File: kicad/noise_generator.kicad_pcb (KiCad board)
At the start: 2 copper layers, 57.2 x 38.1 mm, 12 parts, among them J1 Conn_Coaxial, J2 Connector, U1 LM741

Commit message: Adjustments
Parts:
- moved C1 76.5 mm to (130.4, 82.2)
- moved C2 76.5 mm to (116.6, 88.2)
- moved C3 76.5 mm to (108.4, 79.8)
- moved D1 76.5 mm to (108.8, 82.9)
- moved R1 76.5 mm to (116.5, 73.9)
- moved R2 76.5 mm to (120.1, 88.2)
- moved U1 76.5 mm to (116.6, 77.3)
- moved C4 76.5 mm to (135.4, 79.0)
- moved J1 76.5 mm to (139.7, 82.2)
- moved J2 76.5 mm to (99.4, 81.8)
- moved R3 76.5 mm to (130.3, 91.4)
- moved R4 76.5 mm to (113.5, 76.2)

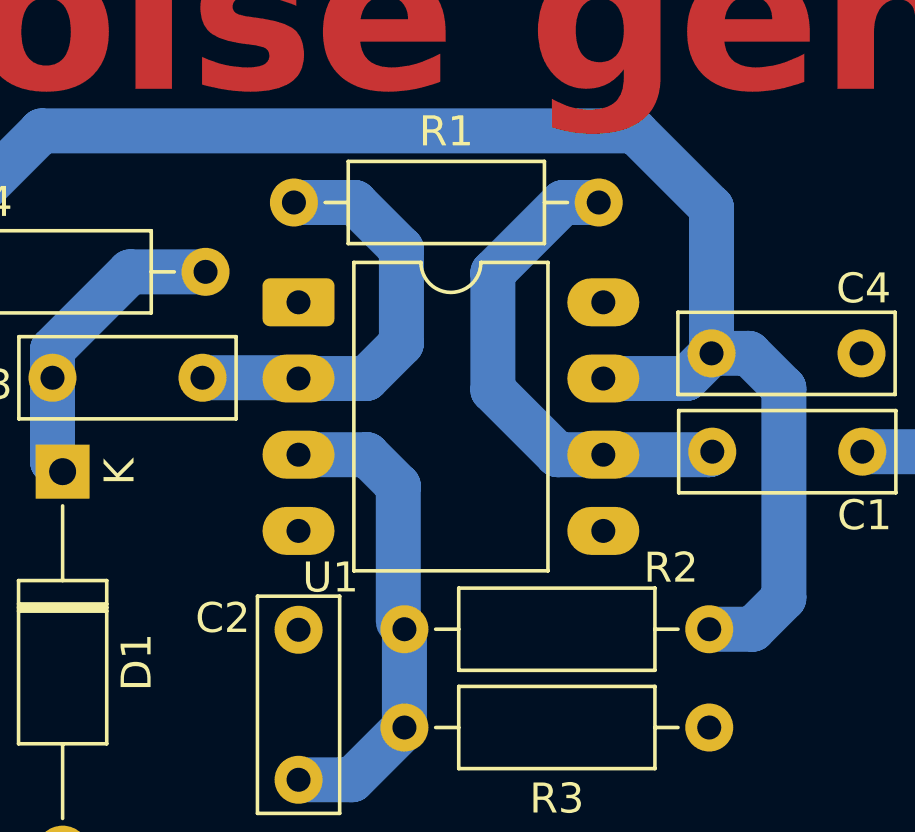
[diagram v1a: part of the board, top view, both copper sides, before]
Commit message: Reduced IC size and updated component values to final
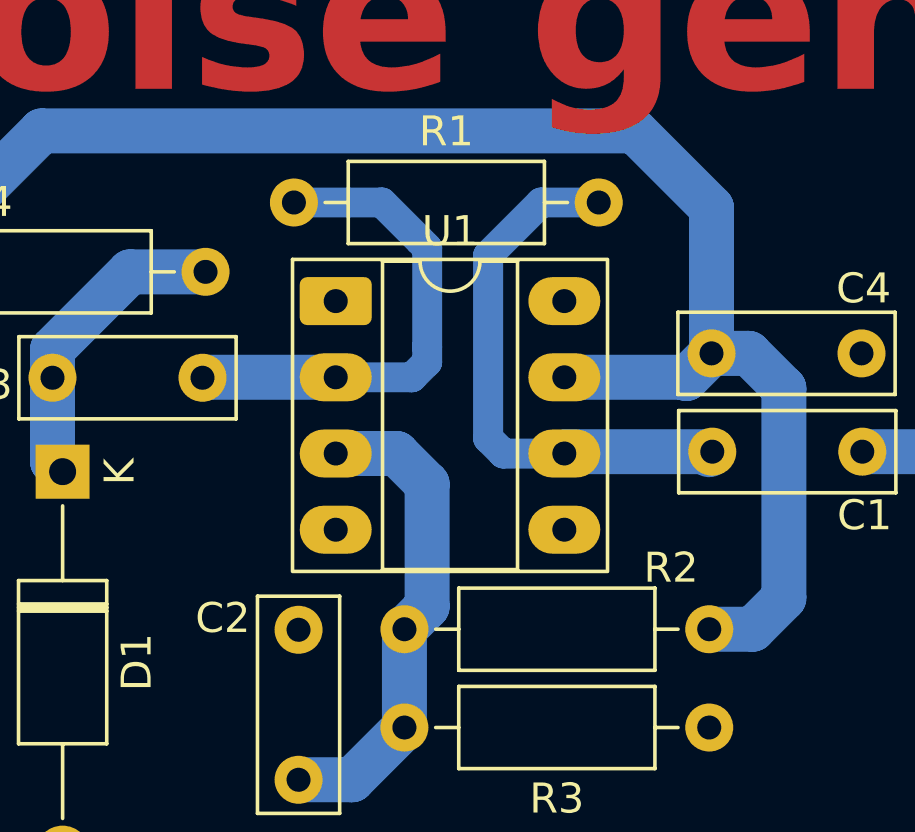
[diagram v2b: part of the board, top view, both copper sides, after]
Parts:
- R1: value 10k -> 100k
- U1: footprint Package_DIP:DIP-8_W10.16mm_LongPads -> Package_DIP:DIP-8_W7.62mm_Socket_LongPads
- moved U1 1.24 mm to (117.9, 77.2)
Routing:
- net Net-(U1--): track 14.5 -> 16.6 mm
- net Net-(C1-Pad1): track 16.7 -> 18.4 mm
- net +9V: track 59.7 -> 61.1 mm
